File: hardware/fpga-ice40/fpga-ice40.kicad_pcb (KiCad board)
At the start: 4 copper layers, 53.3 x 48.6 mm, 91 parts, among them J1 Conn_01x03, J2 MicroSD_Molex_1040310811, J3 Conn_02x05_Odd_Even, J4 Conn_02x05_Odd_Even, J5 USB_B_Micro, J6 Conn_02x20_Odd_Even, Q1 2N7002H, U1 iCE40HX4K-TQ144, U10 SN74LVC1G08DBVR, U2 AZ1117-1.2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

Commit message: Component selection by MPN and routing cleanup
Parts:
- C16: footprint Capacitor_SMD:C_0603_1608Metric -> Capacitor_SMD:C_0805_2012Metric
- C19: value 10n -> 100n
- FB1: value 33R, 500mA -> 33R, 3A
- moved C16 0.29 mm to (140.8, 75.1)
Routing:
- net USB_5V: track 35.1 -> 34.1 mm
- net GND: track 166.2 -> 166.8 mm, vias 74 -> 73

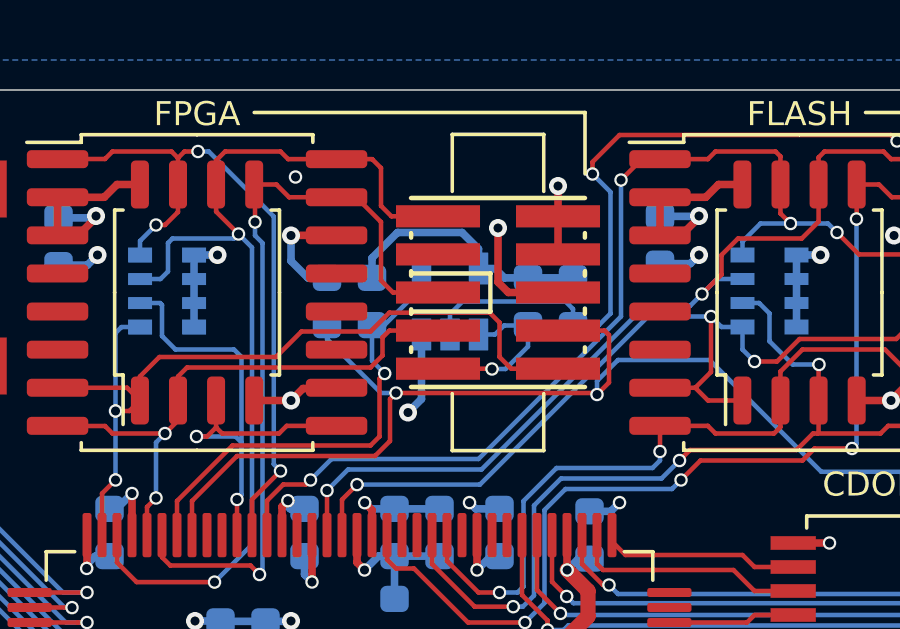
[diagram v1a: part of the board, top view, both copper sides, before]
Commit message: Simplify FPGA reset logic layout with resistor array
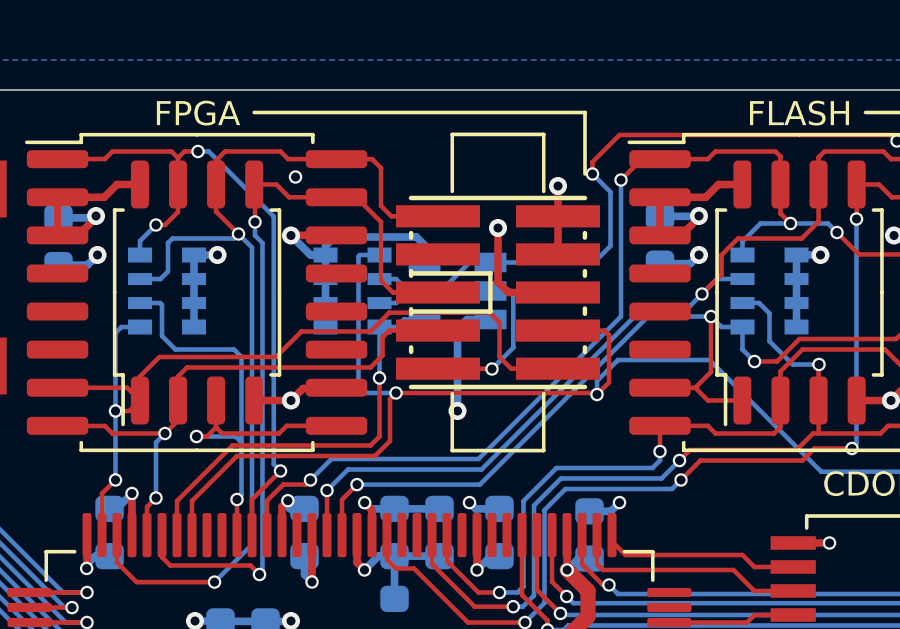
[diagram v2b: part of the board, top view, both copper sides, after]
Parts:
- removed R12, R13, R9: 10k, Resistor_SMD:R_0603_1608Metric
- J3, J4: value Conn_02x05_Odd_Even -> FTSH-105-01-L-DV-K
- Q1: value 2N7002H -> 2N7002H-7
- R8: footprint Resistor_SMD:R_0603_1608Metric -> Resistor_SMD:R_Array_Convex_4x0603
- RN4, RN5, RN6, RN7, RN8, RN9: value 33R -> 33R, 1%
- U10: value SN74LVC1G08DBVR -> MC74HC1G08DTT1G
- U2: value AZ1117-1.2 -> AZ1117-3.3
- U4: value IS42S16320F-6TL -> IS42S16320F-7TL
- X1: value ECS-2520MV-xxx-xx -> 50MHz
- moved R8 0.74 mm to (160.1, 76.2), turned to 180 degrees
- moved U10 0.43 mm to (163.6, 76.2), turned to 180 degrees
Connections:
- R8 pad 1: P3V3 -> FPGA_CDONE
- R8 pad 2: FPGA_CRESETn -> FLASH_CRESETn
- U10 pad 1: CONFIG_CRESETn -> FLASH_CRESETn
- U10 pad 2: FLASH_CRESETn -> CONFIG_CRESETn
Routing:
- net P3V3: track 107.3 -> 103.1 mm
- net CONFIG_CRESETn: track 5.81 -> 9.28 mm
- net FPGA_CDONE: track 46.9 -> 49.8 mm
- net FPGA_CRESETn: track 15.5 -> 14.0 mm
- net GND: track 166.8 -> 168.0 mm
- net FLASH_CRESETn: track 35.0 -> 34.1 mm

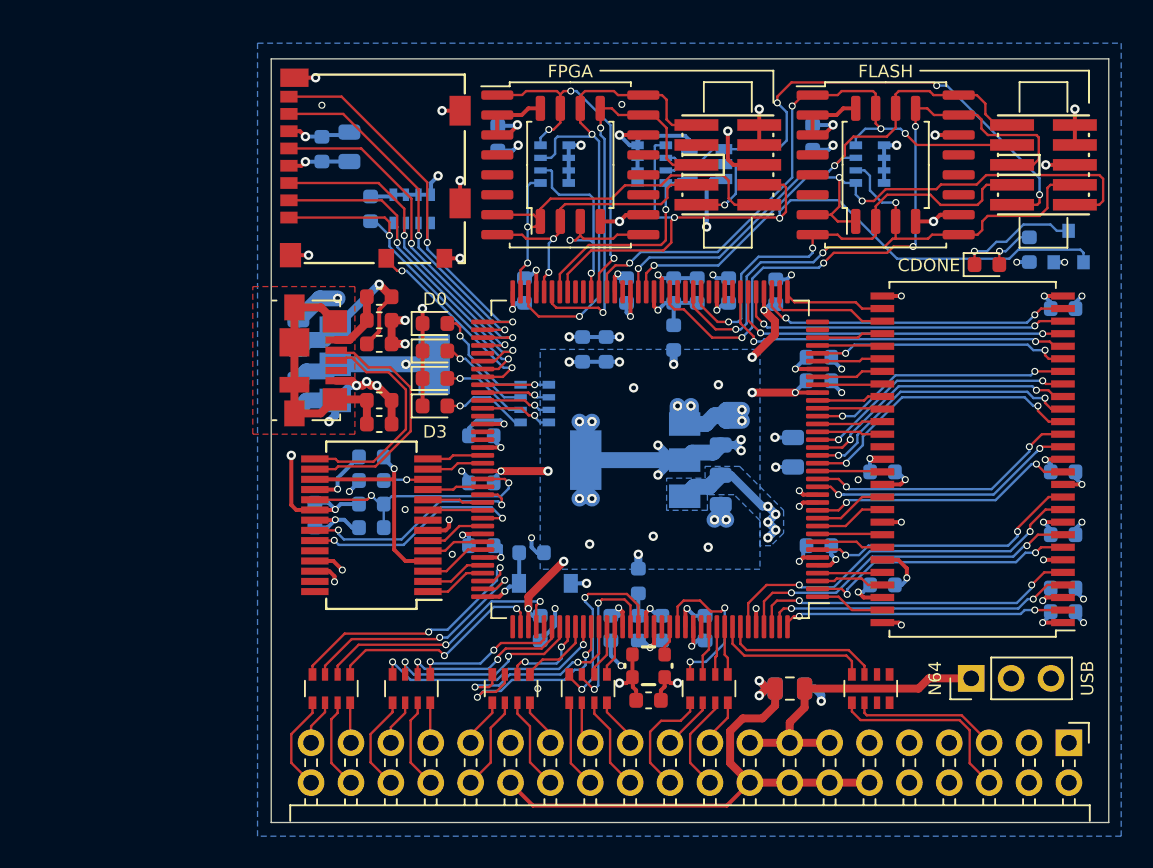
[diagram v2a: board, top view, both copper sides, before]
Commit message: Cleanup CDONE led indicator and add copyright notice
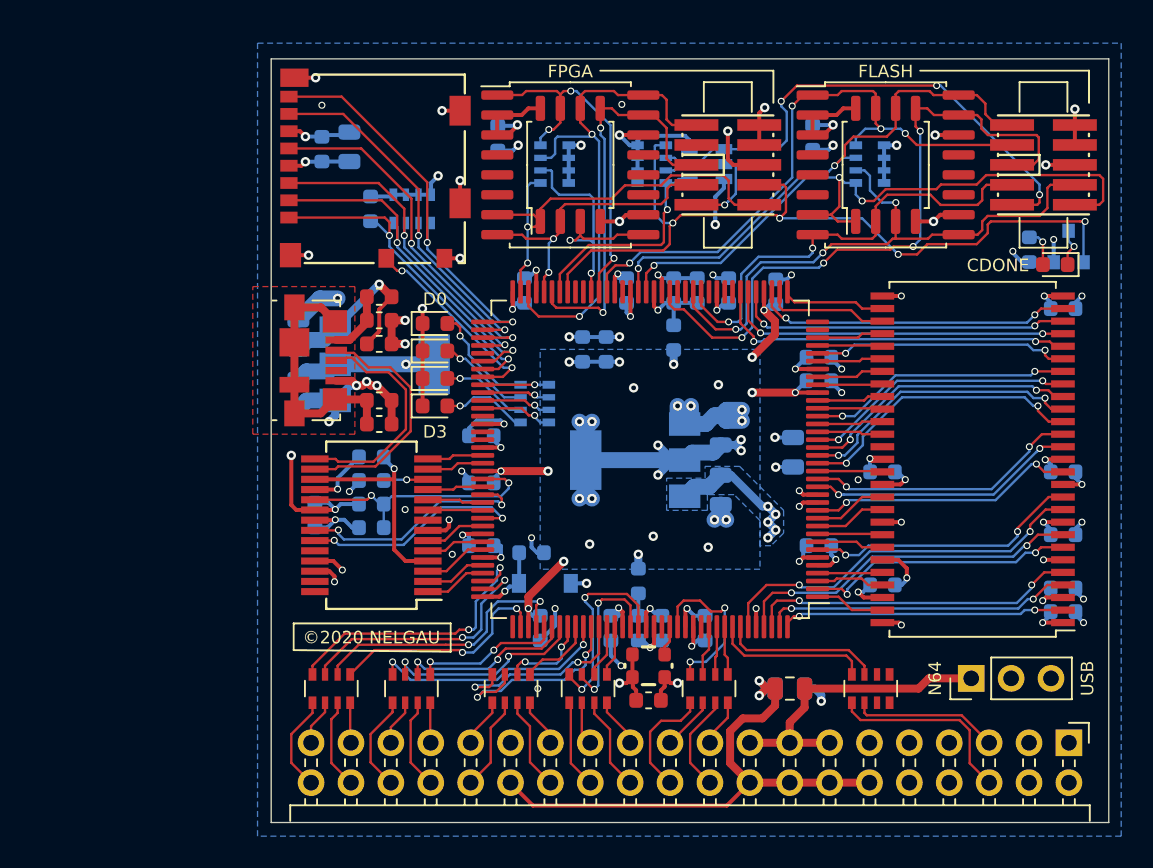
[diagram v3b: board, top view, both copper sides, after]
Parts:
- moved D2 4.35 mm to (185.8, 82.6), turned to 180 degrees
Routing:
- net Net-(D2-Pad1): track 7.73 -> 2.47 mm
- net FPGA_CDONE: track 49.8 -> 51.5 mm, vias 2 -> 4
- net N64_AD0_IC: track 15.9 -> 16.9 mm
- net N64_AD15_IC: track 17.2 -> 18.1 mm
- net FLASH_CRESETn: track 34.1 -> 33.1 mm
- net N64_AD14_IC: track 16.9 -> 17.6 mm
- net Net-(D2-Pad2): track 3.12 -> 2.42 mm
- net P3V3: track 103.1 -> 103.7 mm
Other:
- board text added: "©2020 NELGAU"

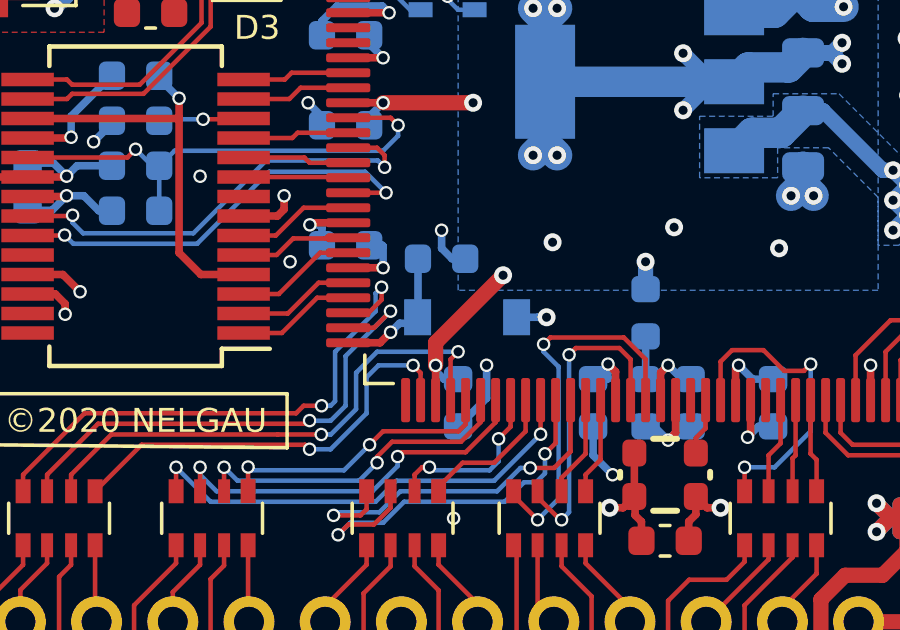
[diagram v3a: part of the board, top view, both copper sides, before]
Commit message: Complete component selection by MPN
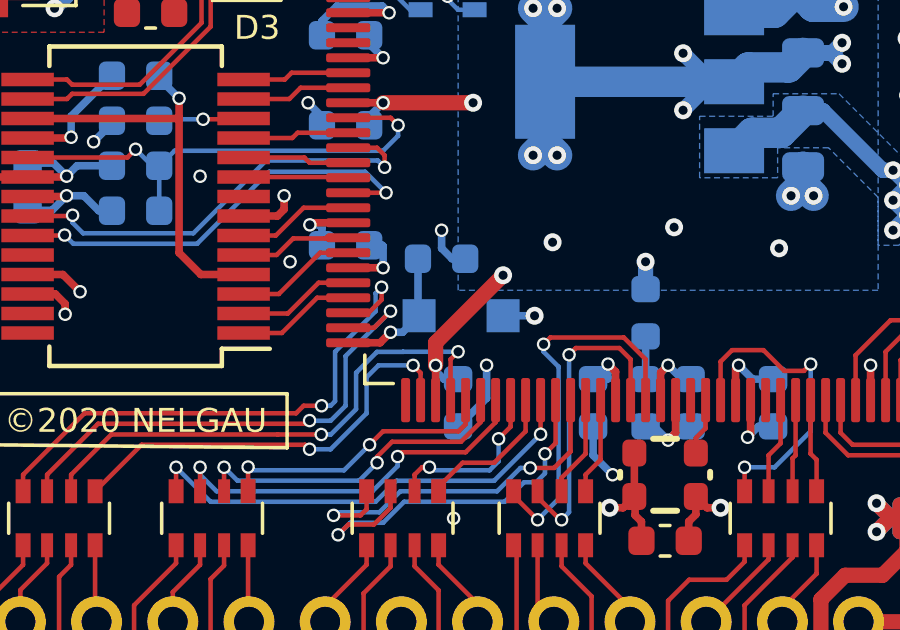
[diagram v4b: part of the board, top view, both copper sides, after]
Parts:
- D1: footprint Diode_SMD:D_SOD-123 -> Diode_SMD:D_SOD-123F
- D2, D3, D4, D5, D6: value Blue -> Green
- R10: value 470R -> 1k
- R11: value 330R -> 1k
- R3: value 6k8 -> 10k
- R5: value 10k -> 20k
- moved D1 0.21 mm to (153.1, 102.8)
- renumbered R8 to RN10

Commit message: Completed verification of all pins for all symbols
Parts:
- added R8: 10k, Resistor_SMD:R_0603_1608Metric, B.Cu at (140.7, 79.0)
- U5, U7: value S25FL256SAGMFI01 -> S25FL256SAGMFI01x
- U6, U8: value W25Q32JVSS -> W25Q32JVSSIM
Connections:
- net SD_CD renamed SD_DET
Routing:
- net SD_DET: track 13.1 -> 18.8 mm
- net P3V3: track 103.7 -> 105.2 mm
- net GND: track 168.1 -> 168.5 mm, vias 73 -> 72

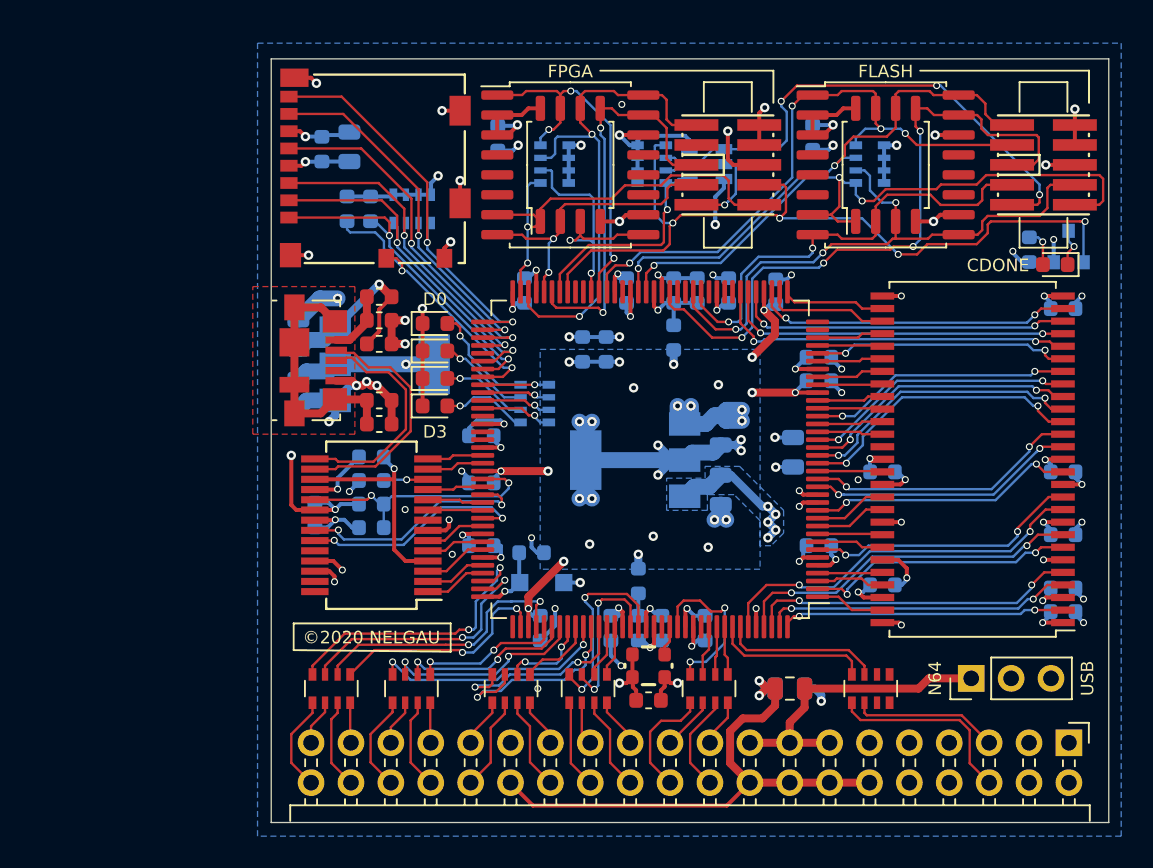
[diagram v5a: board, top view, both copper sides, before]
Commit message: Rename SD_DET signal to SD_CD for consistency
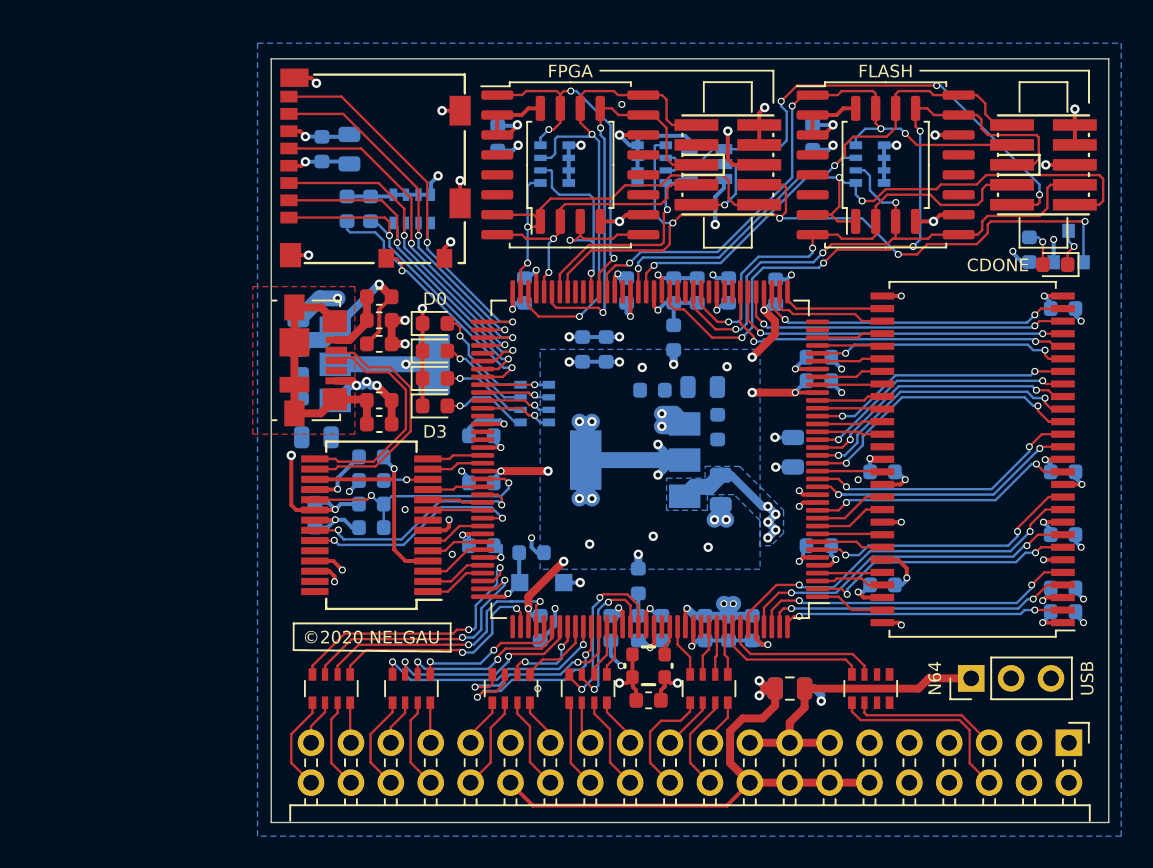
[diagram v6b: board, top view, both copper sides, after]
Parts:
- added C45: 10n, Capacitor_SMD:C_0603_1608Metric, B.Cu at (160.2, 90.6)
- added C46: 1u, Capacitor_SMD:C_0603_1608Metric, B.Cu at (165.0, 105.8)
- added C47: 10n, Capacitor_SMD:C_0603_1608Metric, B.Cu at (166.5, 105.8)
- added R12: R047, Resistor_SMD:R_0603_1608Metric, B.Cu at (164.3, 93.0)
- added R9: R047, Resistor_SMD:R_0603_1608Metric, B.Cu at (137.8, 90.3)
- moved C2 2.98 mm to (138.8, 93.6), turned to 0 degrees
- moved C6 2.98 mm to (163.3, 90.4), turned to 180 degrees
- moved C16 0.15 mm to (140.8, 75.2)
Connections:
- net SD_DET renamed SD_CD
- C2 pad 1: USB_3V3 -> Net-(C2-Pad1)
- C6 pad 1: P1V2 -> Net-(C6-Pad1)
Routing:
- net N64_AD9_IC: track 10.6 -> 3.37 mm, vias 2 -> 0
- net P1V2: track 49.0 -> 43.5 mm, vias 25 -> 23
- net GND: track 168.5 -> 164.0 mm, vias 72 -> 69
- net P3V3: track 105.2 -> 109.6 mm, vias 36 -> 38
- net USB_3V3: track 85.4 -> 82.7 mm
- net N64_AD11_IC: track 12.8 -> 11.8 mm

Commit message: Completed schematic review
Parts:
- C19: value 100n -> 4u7
- R3: value 10k -> 6k8
- R5: value 20k -> 10k
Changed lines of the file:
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@@
     (38 B.Mask user hide)
     (39 F.Mask user hide)
-    (40 Dwgs.User user hide)
+    (40 Dwgs.User user)
     (41 Cmts.User user)
     (42 Eco1.User user hide)
@@
       (effects (font (size 1 1) (thickness 0.15)) (justify mirror))
     )
-    (fp_text value 100n (at 0 -1.43 270) (layer B.Fab)
+    (fp_text value 4u7 (at 0 -1.43 270) (layer B.Fab)
       (effects (font (size 1 1) (thickness 0.15)) (justify mirror))
     )
@@
       (effects (font (size 1 1) (thickness 0.15)) (justify mirror))
     )
-    (fp_text value 20k (at 0 -1.43) (layer B.Fab)
+    (fp_text value 10k (at 0 -1.43) (layer B.Fab)
       (effects (font (size 1 1) (thickness 0.15)) (justify mirror))
     )
@@
       (effects (font (size 1 1) (thickness 0.15)) (justify mirror))
     )
-    (fp_text value 10k (at 0 -1.43) (layer B.Fab)
-      (effects (font (size 1 1) (thickness 0.15)) (justify mirror))
-    )
+    (fp_text value 6k8 (at 0 -1.43) (layer B.Fab)
+      (effects (font (size 1 1) (thickness 0.15)) (justify mirror))
+    )
